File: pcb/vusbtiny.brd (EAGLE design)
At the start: 41.5 x 17 mm, 9 parts, among them IC1 ATtiny45

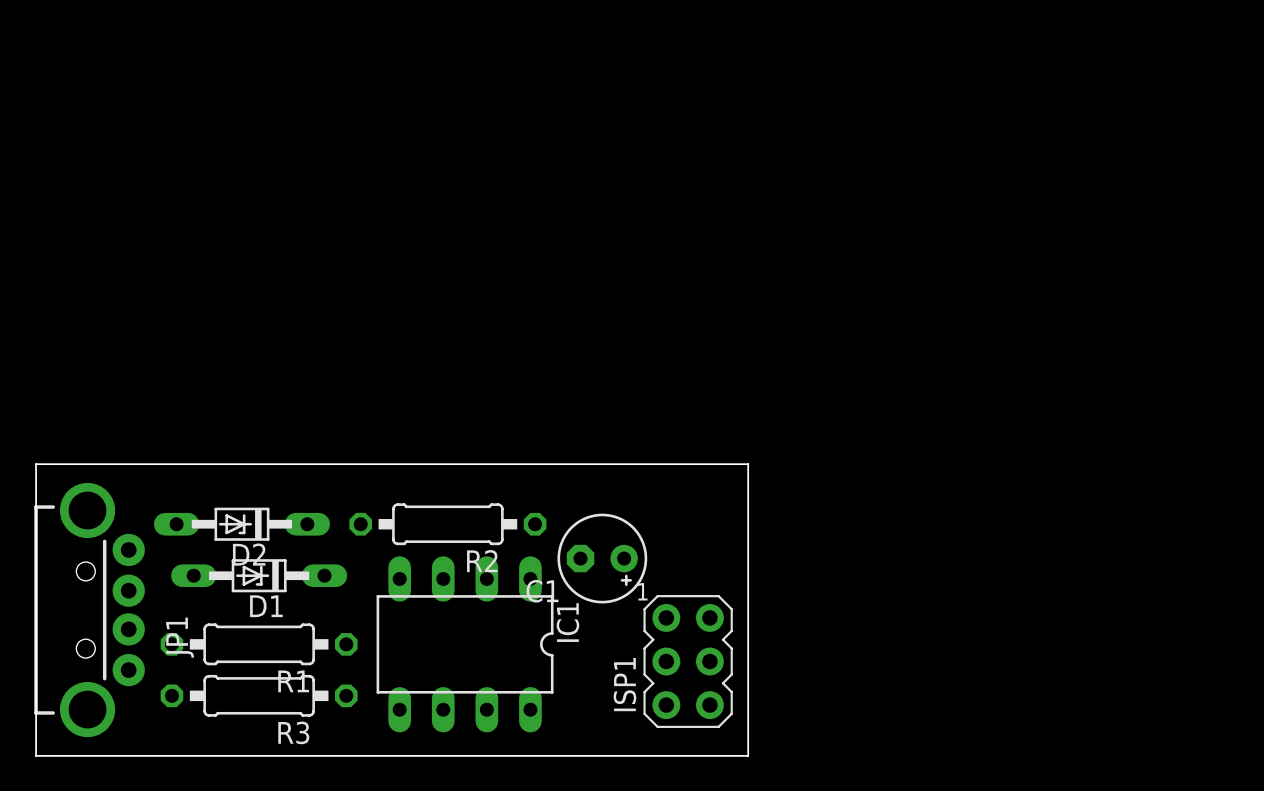
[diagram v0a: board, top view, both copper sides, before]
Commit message: Reposition components to ease routing. Added DRC.
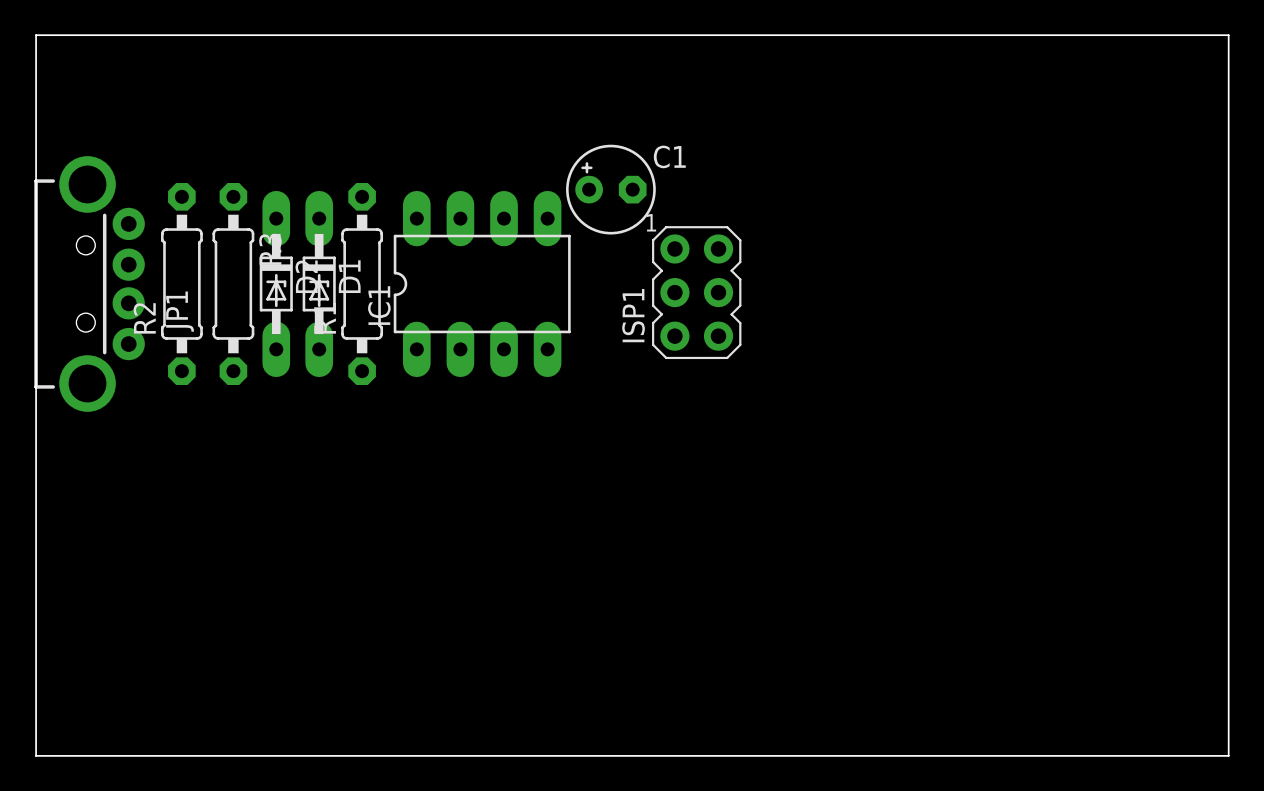
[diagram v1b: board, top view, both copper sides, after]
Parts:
- moved R3 24.0 mm to (11.5, 27.5), turned to 270 degrees
- moved R1 21.8 mm to (19.0, 27.5), turned to 90 degrees
- moved C1 21.5 mm to (33.5, 33.0), turned to 0 degrees
- moved ISP1 21.5 mm to (38.5, 27.0)
- moved IC1 21.0 mm to (26.0, 27.5), turned to 0 degrees
- moved R2 20.9 mm to (8.50, 27.5), turned to 90 degrees
- moved JP1 19.0 mm to (3.00, 27.5)
- moved D1 17.4 mm to (16.5, 27.5), turned to 270 degrees
- moved D2 14.1 mm to (14.0, 27.5), turned to 270 degrees
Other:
- board size 41.5 x 17 mm -> 69.5 x 42 mm

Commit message: Finished routing. Copper pour should be improved.
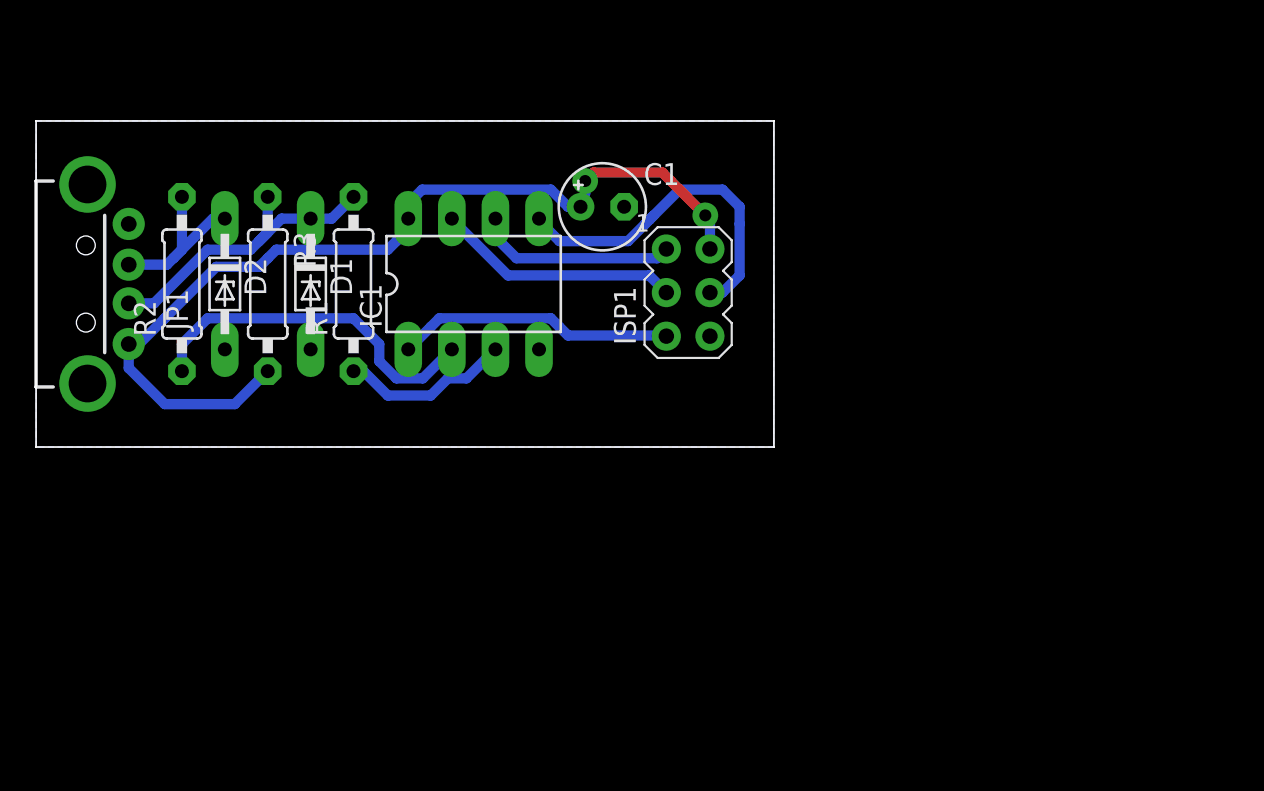
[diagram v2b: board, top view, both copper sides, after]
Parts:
- moved D2 3.00 mm to (11.0, 27.5)
- moved R3 2.00 mm to (13.5, 27.5)
- moved C1 1.12 mm to (33.0, 32.0)
- moved D1 0.50 mm to (16.0, 27.5)
- moved IC1 0.50 mm to (25.5, 27.5)
- moved ISP1 0.50 mm to (38.0, 27.0)
- moved R1 0.50 mm to (18.5, 27.5)
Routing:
- net VCC: track 0.00 -> 54.4 mm, vias 0 -> 2
- net N$3: track 0.00 -> 20.7 mm
- net MOSI: track 0.00 -> 20.5 mm
- net D-: track 0.00 -> 18.5 mm
- net RST: track 0.00 -> 16.2 mm
- net SCK: track 0.00 -> 14.3 mm
- net MISO: track 0.00 -> 11.8 mm
- net D+: track 0.00 -> 10.5 mm
- net N$2: track 0.00 -> 9.97 mm
- added copper zone on layer 16, net GND
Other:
- board size 69.5 x 42 mm -> 43 x 19 mm

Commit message: Finished routing. Wrote script to make board's pdf
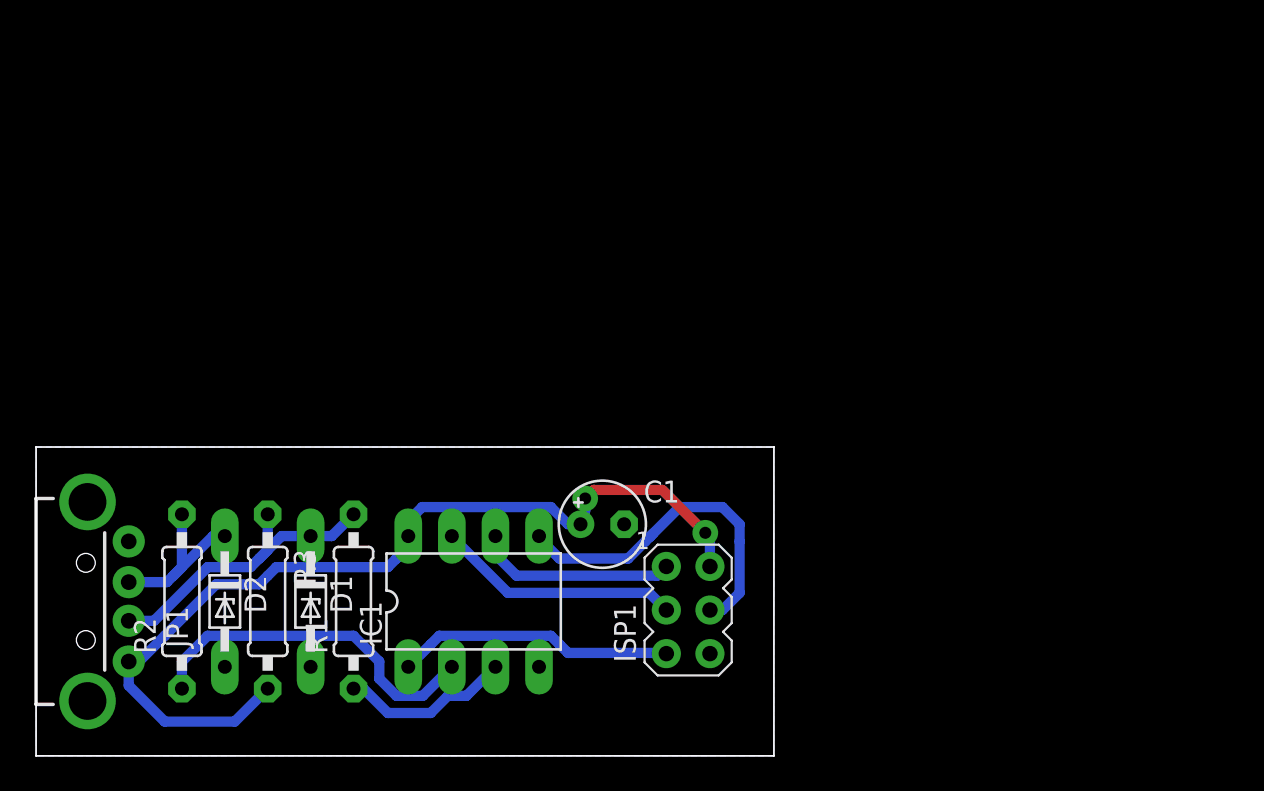
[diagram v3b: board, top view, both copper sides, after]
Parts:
- moved C1 18.5 mm to (33.0, 13.5)
- moved D1 18.5 mm to (16.0, 9.00)
- moved D2 18.5 mm to (11.0, 9.00)
- moved IC1 18.5 mm to (25.5, 9.00)
- moved ISP1 18.5 mm to (38.0, 8.50)
- moved JP1 18.5 mm to (3.00, 9.00)
- moved R1 18.5 mm to (18.5, 9.00)
- moved R2 18.5 mm to (8.50, 9.00)
- moved R3 18.5 mm to (13.5, 9.00)
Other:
- board size 43 x 19 mm -> 43 x 18 mm
